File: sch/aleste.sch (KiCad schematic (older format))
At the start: 11 parts, among them P1 PIN, P2 PIN, P3 PIN, P4 PIN, P5 PIN, P6 PIN, X1 SLOT-62

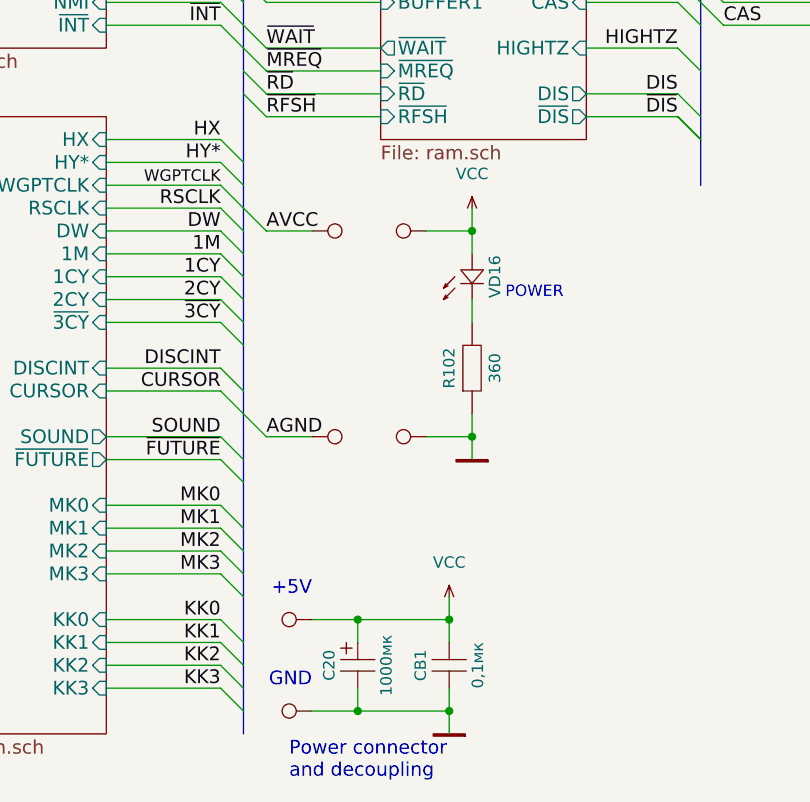
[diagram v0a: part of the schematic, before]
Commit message: More precise version. PCB needs a lot of work.
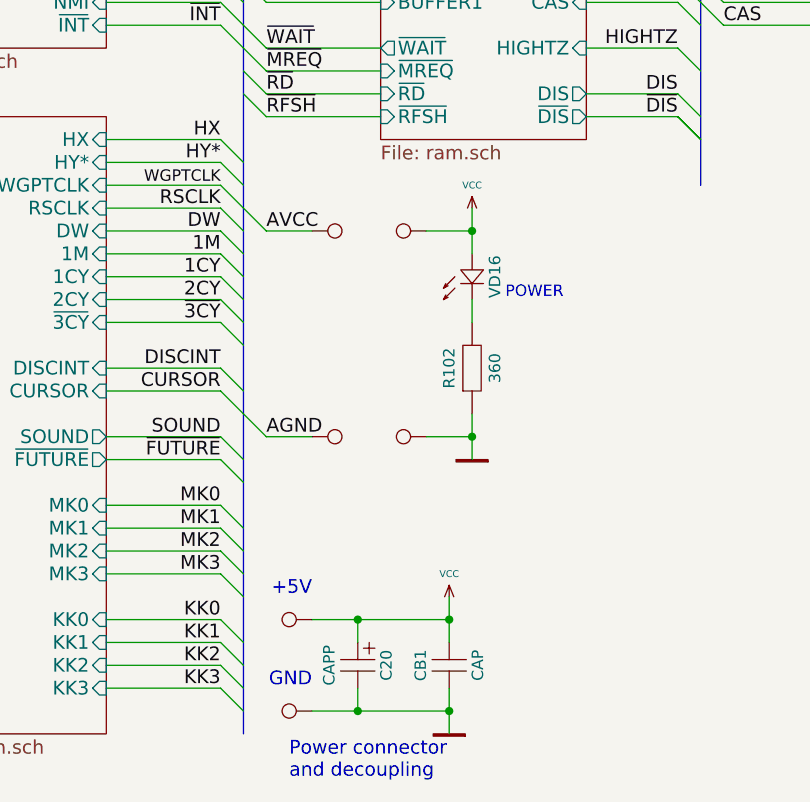
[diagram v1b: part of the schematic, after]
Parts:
- C20: value 1000мк -> CAPP
- CB1: value 0,1мк -> CAP; footprint MyLib:C_Disc_D7.5_P2.5 -> MyLib_metric:C_Disc_D7.5_P2.5
- R102: footprint MyLib:Resistor_Horizontal_RM7.5mm -> MyLib_metric:Resistor_Horizontal_RM7.5mm
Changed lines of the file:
@@
 F 0 "R102" H 6400 5900 50  0000 C CNN
 F 1 "360" H 6400 5700 50  0000 C CNN
-F 2 "MyLib:Resistor_Horizontal_RM7.5mm" H 6400 5750 60  0001 C CNN
+F 2 "MyLib_metric:Resistor_Horizontal_RM7.5mm" H 6400 5750 60  0001 C CNN
 F 3 "" H 6400 5750 60  0000 C CNN
 	1    6400 5800
@@
 	0    -1   1    0
 $EndComp
+$Comp
+L VCC #PWR01
+U 1 1 568C380C
+P 6400 5100
+F 0 "#PWR01" H 6400 5200 30  0001 C CNN
+F 1 "VCC" H 6400 5200 30  0000 C CNN
+F 2 "" H 6400 5100 60  0000 C CNN
+F 3 "" H 6400 5100 60  0000 C CNN
+	1    6400 5100
+	-1   0    0    -1
+$EndComp
 Wire Wire Line
 	6400 5600 6400 5500
@@
 	6400 5100 6400 5300
 $Comp
-L GND #PWR01
+L GND #PWR02
 U 1 1 568C3814
 P 6400 6200
-F 0 "#PWR01" H 6400 6200 30  0001 C CNN
+F 0 "#PWR02" H 6400 6200 30  0001 C CNN
 F 1 "GND" H 6400 6130 30  0001 C CNN
 F 2 "" H 6400 6200 60  0000 C CNN
@@
 D1
 $Comp
-L VCC #PWR02
+L VCC #PWR03
 U 1 1 5683BA2D
 P 1700 3600
-F 0 "#PWR02" H 1700 3700 30  0001 C CNN
+F 0 "#PWR03" H 1700 3700 30  0001 C CNN
 F 1 "VCC" H 1700 3700 30  0000 C CNN
 F 2 "" H 1700 3600 60  0000 C CNN
@@
 L.PEN
 $Comp
-L GND #PWR03
+L GND #PWR04
 U 1 1 56856E40
 P 1700 5800
-F 0 "#PWR03" H 1700 5800 30  0001 C CNN
+F 0 "#PWR04" H 1700 5800 30  0001 C CNN
 F 1 "GND" H 1700 5730 30  0001 C CNN
 F 2 "" H 1700 5800 60  0000 C CNN
@@
 	3200 1200 3000 1200
 $Comp
-L GND #PWR04
+L GND #PWR05
 U 1 1 568FD14B
 P 3100 1000
-F 0 "#PWR04" H 3100 1000 30  0001 C CNN
+F 0 "#PWR05" H 3100 1000 30  0001 C CNN
 F 1 "GND" H 3100 930 30  0001 C CNN
 F 2 "" H 3100 1000 60  0000 C CNN
@@
 P 5900 7100
 F 0 "C20" H 5900 7225 50  0000 C CNN
-F 1 "1000мк" H 5900 6975 50  0000 C CNN
+F 1 "CAPP" H 5900 6975 50  0000 C CNN
 F 2 "Capacitors_ThroughHole:C_Radial_D10_L16_P5" H 5900 7050 60  0001 C CNN
 F 3 "" H 5900 7050 60  0000 C CNN
 	1    5900 7100
-	0    -1   1    0
+	0    1    1    0
 $EndComp
 Wire Wire Line
@@
 P 6300 7100
 F 0 "CB1" H 6300 7225 50  0000 C CNN
-F 1 "0,1мк" H 6300 6975 50  0000 C CNN
-F 2 "MyLib:C_Disc_D7.5_P2.5" H 6300 7050 60  0001 C CNN
+F 1 "CAP" H 6300 6975 50  0000 C CNN
+F 2 "MyLib_metric:C_Disc_D7.5_P2.5" H 6300 7050 60  0001 C CNN
 F 3 "" H 6300 7050 60  0000 C CNN
 	1    6300 7100
@@
 $EndComp
 $Comp
-L GND #PWR05
+L GND #PWR06
 U 1 1 56725302
 P 6300 7400
-F 0 "#PWR05" H 6300 7400 30  0001 C CNN
+F 0 "#PWR06" H 6300 7400 30  0001 C CNN
 F 1 "GND" H 6300 7330 30  0001 C CNN
 F 2 "" H 6300 7400 60  0000 C CNN
@@
 	-1   0    0    -1
 $EndComp
+$Comp
+L VCC #PWR07
+U 1 1 567260FF
+P 6300 6800
+F 0 "#PWR07" H 6300 6900 30  0001 C CNN
+F 1 "VCC" H 6300 6900 30  0000 C CNN
+F 2 "" H 6300 6800 60  0000 C CNN
+F 3 "" H 6300 6800 60  0000 C CNN
+	1    6300 6800
+	-1   0    0    -1
+$EndComp
 Entry Wire Line
 	3300 7000 3400 7100
@@
 Wire Wire Line
 	9300 3900 9700 3900
-$Comp
-L VCC #PWR06
-U 1 1 56E324C8
-P 6300 6800
-F 0 "#PWR06" H 6300 6650 50  0001 C CNN
-F 1 "VCC" H 6300 6950 50  0000 C CNN
-F 2 "" H 6300 6800 50  0000 C CNN
-F 3 "" H 6300 6800 50  0000 C CNN
-	1    6300 6800
-	1    0    0    -1
-$EndComp
-$Comp
-L VCC #PWR07
-U 1 1 56E332ED
-P 6400 5100
-F 0 "#PWR07" H 6400 4950 50  0001 C CNN
-F 1 "VCC" H 6400 5250 50  0000 C CNN
-F 2 "" H 6400 5100 50  0000 C CNN
-F 3 "" H 6400 5100 50  0000 C CNN
-	1    6400 5100
-	1    0    0    -1
-$EndComp
 $EndSCHEMATC

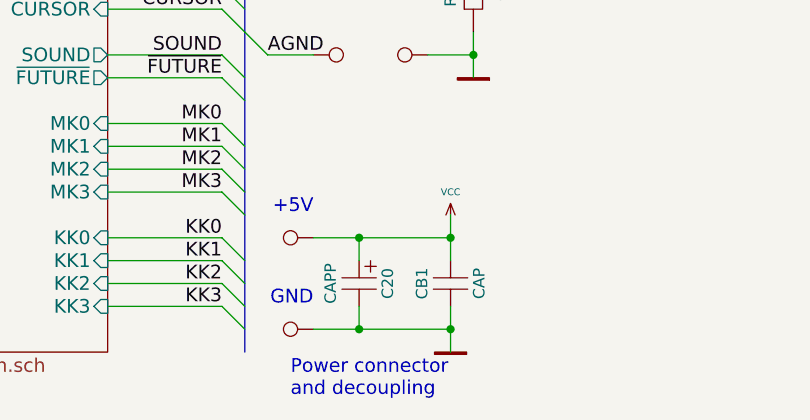
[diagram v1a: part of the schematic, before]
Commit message: IR22 and IR23 symbols updated, part values updated
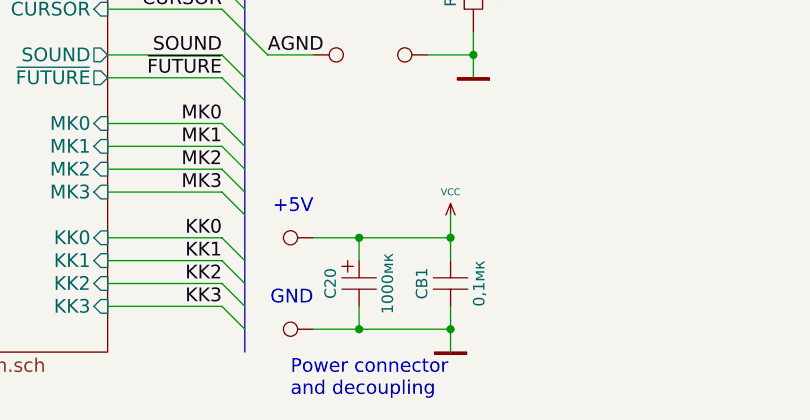
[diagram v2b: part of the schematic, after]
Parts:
- C20: value CAPP -> 1000мк
- CB1: value CAP -> 0,1мк
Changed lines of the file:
@@
 P 5900 7100
 F 0 "C20" H 5900 7225 50  0000 C CNN
-F 1 "CAPP" H 5900 6975 50  0000 C CNN
+F 1 "1000мк" H 5900 6975 50  0000 C CNN
 F 2 "Capacitors_ThroughHole:C_Radial_D10_L16_P5" H 5900 7050 60  0001 C CNN
 F 3 "" H 5900 7050 60  0000 C CNN
 	1    5900 7100
-	0    1    1    0
+	0    -1   1    0
 $EndComp
 Wire Wire Line
@@
 P 6300 7100
 F 0 "CB1" H 6300 7225 50  0000 C CNN
-F 1 "CAP" H 6300 6975 50  0000 C CNN
+F 1 "0,1мк" H 6300 6975 50  0000 C CNN
 F 2 "MyLib_metric:C_Disc_D7.5_P2.5" H 6300 7050 60  0001 C CNN
 F 3 "" H 6300 7050 60  0000 C CNN

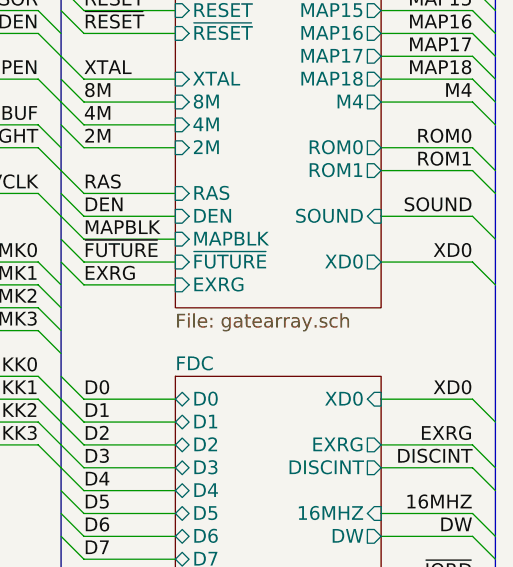
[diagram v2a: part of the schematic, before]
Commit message: Board fully redrawn
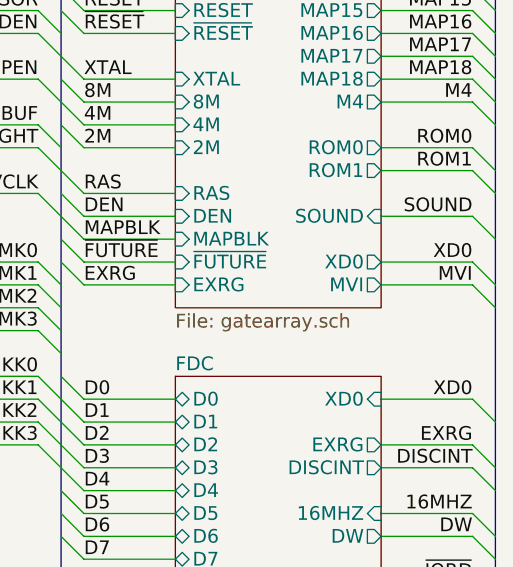
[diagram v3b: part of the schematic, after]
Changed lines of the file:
@@
 F55 "XD0" O R 10600 4200 60
 F56 "RAS" I L 9700 3900 60
+F57 "MVI" O R 10600 4300 60
 $EndSheet
 $Sheet
@@
 Wire Wire Line
 	9300 3900 9700 3900
+Wire Wire Line
+	10600 4300 11000 4300
+Text Label 11000 4300 2    60   ~ 0
+MVI
+Entry Wire Line
+	11000 4300 11100 4400
 $EndSCHEMATC
